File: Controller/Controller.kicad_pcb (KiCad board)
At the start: 4 copper layers, 65 x 56 mm, 62 parts, among them CN1 SERVO_PWM, CN10 FEMALE_LEFT, CN11 FEMALE_RIGHT, CN2 CFG1, CN3 CFG1, CN4 CFG1, CN5 FEMALE_LEFT, CN6 FEMALE_RIGHT, CN7 CFG1, CN8 CFG1, CN9 CFG1, J1 PJ-202AH, J10 ICSP, J11 MotorTerm, J12 MotorHeader, J13 MotorTerm, J14 MotorHeader, J15 UJ2-BH-1-TH, J2 TermLaser, J3 TermStop, J4 LASER_PWR, J5 LASER_PULSE, J6 TermControl, J7 TermLimit, J8 TermAux, J9 ConnPi, K1 SW_RESET, U1 CJ7805, U2 INTERFACE-CH340T_SSOP20_, U3 MCU-ATMEGA328P-AU_TQFP32_, Y1 12MHz, Y2 16MHZ

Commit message: Probably giving up on Pi option
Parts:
- J15: footprint UJ2-BH-1-TH:CUI_UJ2-BH-1-TH -> CUI:CUI_UJ2-BH-1-TH
- moved J10 229.9 mm to (96.5, 47.6)
- moved R1 200.7 mm to (59.1, 105.6)
- moved CN1 200.7 mm to (52.6, 106.4)
- moved J3 200.7 mm to (36.9, 92.2)
- moved J4 200.7 mm to (63.0, 90.1)
- moved J5 200.7 mm to (63.0, 94.1)
- moved J6 200.7 mm to (49.5, 92.2)
- moved J7 200.7 mm to (37.8, 100.4)
- moved J8 200.7 mm to (37.8, 108.7)
- moved C5 198.8 mm to (114.8, 91.4), turned to 90 degrees
- moved C3 196.3 mm to (106.9, 91.4), turned to 90 degrees
- moved C7 196.0 mm to (108.4, 56.9)
- moved R3 196.0 mm to (107.9, 61.8)
- moved C11 196.0 mm to (98.9, 67.4)
- moved C4 196.0 mm to (84.2, 70.8)
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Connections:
- J11 pad 1: Net-(CN6-Pad3) -> Net-(CN6-Pad6)
- J11 pad 2: Net-(CN6-Pad4) -> Net-(CN6-Pad5)
- J11 pad 3: Net-(CN6-Pad5) -> Net-(CN6-Pad4)
- J11 pad 4: Net-(CN6-Pad6) -> Net-(CN6-Pad3)
- J12 pad 1: Net-(CN6-Pad3) -> Net-(CN6-Pad6)
- J12 pad 2: Net-(CN6-Pad4) -> Net-(CN6-Pad5)
- J12 pad 3: Net-(CN6-Pad5) -> Net-(CN6-Pad4)
- J12 pad 4: Net-(CN6-Pad6) -> Net-(CN6-Pad3)
- J13 pad 1: Net-(CN11-Pad3) -> Net-(CN11-Pad6)
- J13 pad 2: Net-(CN11-Pad4) -> Net-(CN11-Pad5)
- J13 pad 3: Net-(CN11-Pad5) -> Net-(CN11-Pad4)
- J13 pad 4: Net-(CN11-Pad6) -> Net-(CN11-Pad3)
- J14 pad 1: Net-(CN11-Pad3) -> Net-(CN11-Pad6)
- J14 pad 2: Net-(CN11-Pad4) -> Net-(CN11-Pad5)
- J14 pad 3: Net-(CN11-Pad5) -> Net-(CN11-Pad4)
- J14 pad 4: Net-(CN11-Pad6) -> Net-(CN11-Pad3)
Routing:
- net GND: track 0.00 -> 35.2 mm
- net Net-(J15-Pad3): track 0.00 -> 10.4 mm
- net Net-(C3-Pad2): track 0.00 -> 9.46 mm
- net /VIN_12V: track 0.00 -> 9.07 mm
- net Net-(J15-Pad2): track 0.00 -> 7.28 mm
- net Net-(C5-Pad2): track 0.00 -> 6.24 mm
- net 5V: track 0.00 -> 2.63 mm
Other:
- net class 5V: via_dia 0.8 -> 1.2; via_drill 0.4 -> 0.6

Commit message: More power routing
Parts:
- removed J9: ConnPi, Connector_PinHeader_2.54mm:PinHeader_1x05_P2.54mm_Vertical
- added D3: LED_BLUE, OPL_Optoelectronics:LED-0603, F.Cu at (210.2, 35.6)
- added R7: 220R, OPL_Resistor:R0603, F.Cu at (210.2, 32.4)
- moved H1 150.9 mm to (215.9, 34.3)
- moved J3 142.1 mm to (172.3, 49.4), turned to 180 degrees
- moved J1 133.4 mm to (209.6, 59.7), turned to 270 degrees
- moved C1 123.3 mm to (203.5, 55.9), turned to 270 degrees
- moved U1 112.4 mm to (198.6, 58.9), turned to 270 degrees
- moved C4 111.5 mm to (193.4, 48.1), turned to 180 degrees
- moved D2 107.9 mm to (205.1, 35.6), turned to 270 degrees
- moved C2 104.9 mm to (193.8, 55.9), turned to 270 degrees
- moved D1 103.8 mm to (207.6, 35.6), turned to 270 degrees
- moved Y2 99.6 mm to (180.3, 35.4), turned to 180 degrees
- moved R5 98.7 mm to (207.6, 32.4), turned to 90 degrees
- moved U2 97.4 mm to (198.5, 42.5)
- moved Y1 97.1 mm to (198.5, 50.0)
- moved J15 97.1 mm to (205.5, 43.8)
- moved C3 96.6 mm to (194.6, 50.8)
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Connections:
- J3 pad 1: /GRBL_ABORT -> /NANO_RESET
- J3 pad 3: /NANO_RESET -> /GRBL_ABORT
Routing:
- net GND: track 35.2 -> 163.3 mm, vias 0 -> 4
- net 5V: track 2.63 -> 64.4 mm, vias 0 -> 4
- net /NANO_RESET: track 0.00 -> 16.7 mm
- net Net-(C12-Pad1): track 0.00 -> 6.43 mm, vias 0 -> 3
- net /GRBL_RX: track 0.00 -> 6.37 mm
- net /Arduino Nano/USB_RX: track 0.00 -> 6.32 mm
- net Net-(C8-Pad2): track 0.00 -> 5.96 mm
- net Net-(C7-Pad1): track 0.00 -> 5.94 mm
- net /GRBL_TX: track 0.00 -> 5.55 mm
- net Net-(C4-Pad1): track 0.00 -> 5.27 mm
- net /Arduino Nano/USB_TX: track 0.00 -> 5.04 mm
- net Net-(D3-Pad1): track 0.00 -> 1.65 mm
- net Net-(D2-Pad1): track 0.00 -> 1.65 mm
- net Net-(D1-Pad1): track 0.00 -> 1.65 mm
- net Net-(C3-Pad2): track 9.46 -> 8.31 mm
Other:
- board outline removed
- board text added: "PWR"
- board text added: "RX"
- board text added: "TX"

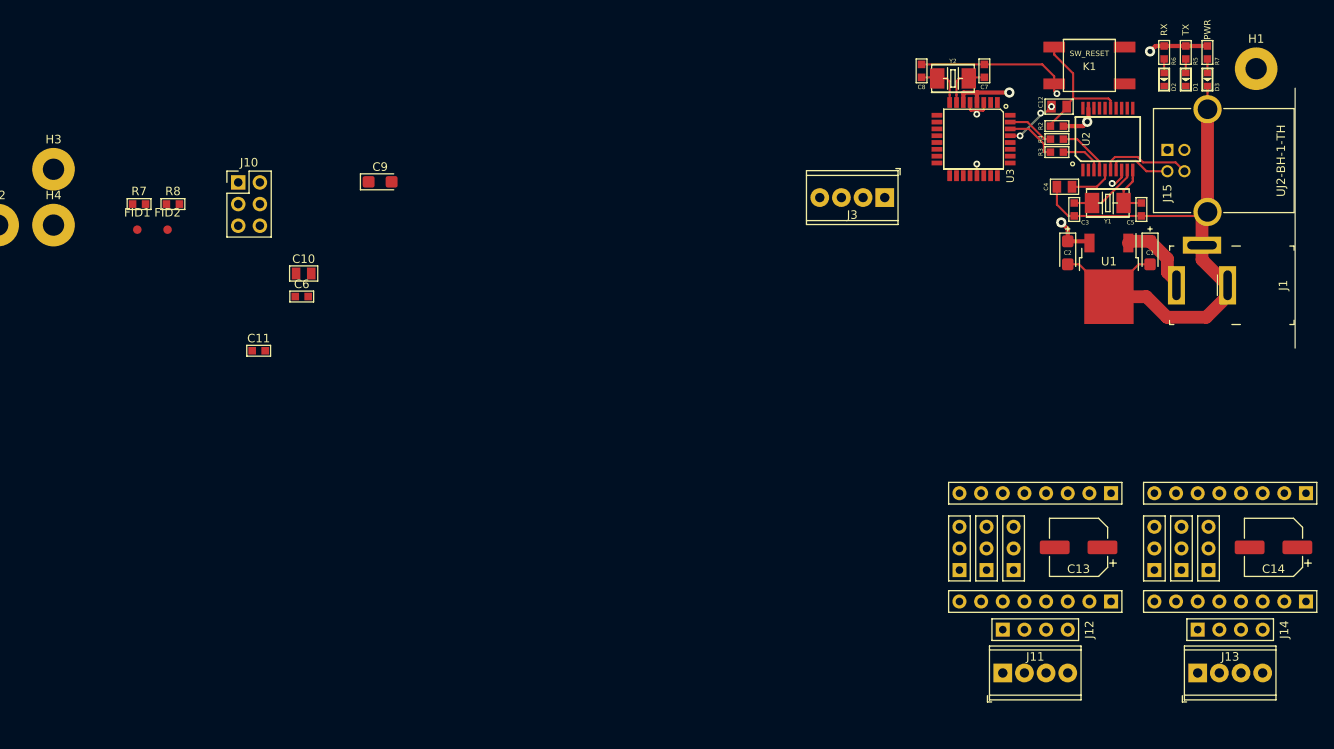
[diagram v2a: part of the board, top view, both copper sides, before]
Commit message: power and nano cleanup
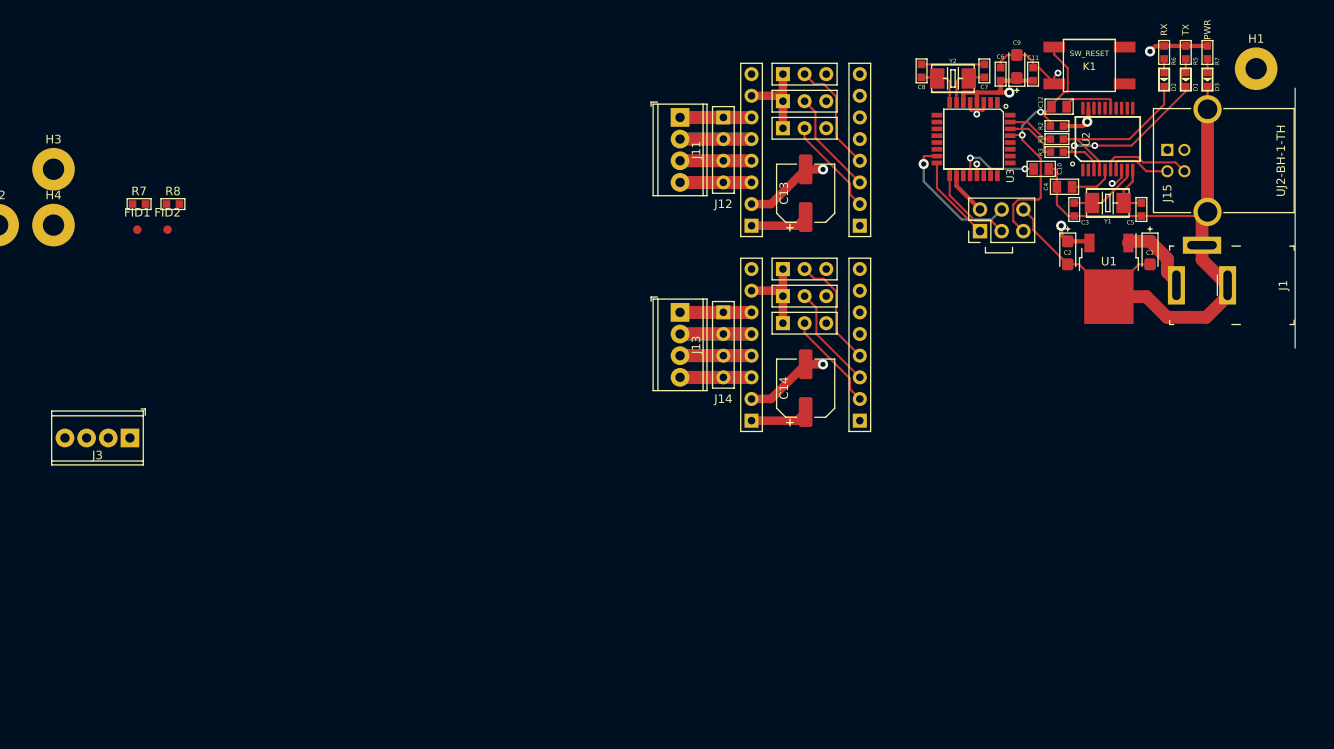
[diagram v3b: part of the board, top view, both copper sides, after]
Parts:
- moved C11 96.4 mm to (189.7, 34.9), turned to 270 degrees
- moved J3 92.9 mm to (83.8, 77.6)
- moved C10 87.4 mm to (190.7, 46.0)
- moved J10 87.2 mm to (183.5, 53.3), turned to 90 degrees
- moved C6 86.0 mm to (185.9, 34.9), turned to 270 degrees
- moved C9 75.9 mm to (187.8, 34.0), turned to 90 degrees
- moved J11 75.3 mm to (148.3, 40.0), turned to 270 degrees
- moved J13 74.0 mm to (148.3, 62.9), turned to 270 degrees
- moved J14 68.2 mm to (153.4, 66.7), turned to 90 degrees
- moved J12 67.1 mm to (153.4, 43.8), turned to 90 degrees
- moved CN11 63.7 mm to (156.7, 66.7), turned to 270 degrees
- moved CN6 62.5 mm to (156.7, 43.8), turned to 270 degrees
- moved CN4 58.5 mm to (162.9, 34.9), turned to 180 degrees
- moved C14 58.0 mm to (163.1, 71.8), turned to 90 degrees
- moved CN3 56.6 mm to (162.9, 38.1), turned to 180 degrees
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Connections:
- C12 pad 1: Net-(C12-Pad1) -> /NANO_RESET
- C12 pad 2: /NANO_RESET -> Net-(C12-Pad2)
- U2 pad 15: /NANO_RESET -> Net-(C12-Pad2)
- U3 pad 29: Net-(C12-Pad1) -> /NANO_RESET
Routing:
- net GND: track 163.3 -> 238.3 mm, vias 4 -> 6
- net 5V: track 64.4 -> 105.6 mm
- net /Arduino Nano/USB_TX: track 5.04 -> 22.3 mm, vias 0 -> 2
- net Net-(CN6-Pad6): track 0.00 -> 16.8 mm
- net Net-(CN6-Pad5): track 0.00 -> 16.8 mm
- net Net-(CN6-Pad4): track 0.00 -> 16.8 mm
- net Net-(CN6-Pad3): track 0.00 -> 16.8 mm
- net Net-(CN11-Pad6): track 0.00 -> 16.8 mm
- net Net-(CN11-Pad5): track 0.00 -> 16.8 mm
- net Net-(CN11-Pad4): track 0.00 -> 16.8 mm
- net Net-(CN11-Pad3): track 0.00 -> 16.8 mm
- net /NANO_RESET: track 16.7 -> 33.0 mm, vias 0 -> 2
- net /PULSE: track 0.00 -> 15.9 mm, vias 0 -> 1
- net /Arduino Nano/USB_RX: track 6.32 -> 22.0 mm
- net /VIN_12V: track 9.07 -> 22.6 mm
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
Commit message: Mostly final layout
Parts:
- removed the R7 at (84.9, 50.2)
- removed R8: 2K, OPL_Resistor:R0603
- moved J6 153.6 mm to (202.6, 79.4)
- moved H4 144.6 mm to (216.5, 81.5)
- moved CN1 136.0 mm to (182.2, 65.4)
- moved R1 134.7 mm to (183.6, 54.2), turned to 90 degrees
- moved J8 131.9 mm to (166.4, 79.4)
- moved J2 130.5 mm to (178.4, 79.4)
- moved J5 123.8 mm to (184.8, 71.8), turned to 90 degrees
- moved FID2 122.9 mm to (210.0, 70.0)
- moved J7 118.4 mm to (154.3, 79.4)
- moved J4 118.2 mm to (179.7, 71.8), turned to 90 degrees
- moved J3 106.7 mm to (190.5, 79.4), turned to 0 degrees
- moved H2 85.2 mm to (148.5, 81.5)
- moved H3 75.1 mm to (148.5, 31.5)
- moved FID1 65.4 mm to (150.0, 51.0)
- moved J10 6.08 mm to (178.2, 50.4), turned to 0 degrees
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- renumbered J15 to J9
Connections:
- J6 pad 1: /START -> /HOLD
- J6 pad 3: /HOLD -> /START
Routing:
- net GND: track 238.3 -> 364.7 mm, vias 6 -> 8
- net /X_LIMIT: track 0.00 -> 58.3 mm
- net /Y_LIMIT: track 0.00 -> 52.2 mm
- net /START: track 0.00 -> 44.0 mm
- net /HOLD: track 0.00 -> 39.6 mm
- net /GRBL_ABORT: track 0.00 -> 37.0 mm
- net /STEP_EN: track 0.00 -> 36.2 mm
- net /NANO_RESET: track 33.0 -> 66.3 mm, vias 2 -> 3
- net /PULSE: track 15.9 -> 48.9 mm, vias 1 -> 0
- net /Y_STEP: track 0.00 -> 32.1 mm, vias 0 -> 1
- net /X_STEP: track 0.00 -> 27.2 mm
- net /Y_DIR: track 0.00 -> 19.3 mm
- net /X_DIR: track 0.00 -> 12.1 mm
- net 5V: track 105.6 -> 111.9 mm, vias 4 -> 5
- net /Arduino Nano/D12: track 10.1 -> 5.19 mm
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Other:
- board outline added: 75 x 57 mm
- board text added: "12V"
- board text added: "5V"
- board text added: "ABORT"
- board text added: "AUX POWER"
- board text added: "CONTROL"
- board text added: "G"
- board text added: "GND"
- board text added: "HOLD"
- board text added: "LASER"
- board text added: "LIMITS"
- board text added: "PWM"
- board text added: "RESET"
- board text added: "SERVO"
- board text added: "START"
- board text added: "X"
- board text added: "Y"

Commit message: Near complete layout
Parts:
- moved H1 0.35 mm to (216.8, 31.2)
- moved H2 0.35 mm to (148.2, 81.8)
- moved H3 0.35 mm to (148.2, 31.2)
- moved H4 0.35 mm to (216.8, 81.8)
- moved C8 0.25 mm to (176.4, 34.5)
- moved C7 0.25 mm to (184.3, 34.5)
- moved J12 0.13 mm to (155.4, 40.0)
- moved J14 0.13 mm to (155.4, 61.6)
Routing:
- net GND: track 364.7 -> 529.1 mm
- net /VIN_12V: track 22.6 -> 120.8 mm
- net 5V: track 111.9 -> 171.2 mm
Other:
- board text added: "A+"
- board text added: "A-"
- board text added: "B+"
- board text added: "B-"
- board text added: "X MOTOR"
- board text added: "Y MOTOR"

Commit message: Beta v1
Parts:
- added G***: LOGO, Logos:logo_MLlabs_small, F.Cu at (190.5, 60.0)
- added J15: 12V_TERM, OPL_Connector:H2-5.0-10.5X8.0MM, F.Cu at (215.8, 70.5)
- moved FID2 5.83 mm to (205.0, 73.0)
- moved CN2 0.51 mm to (164.3, 37.5)
- moved CN3 0.51 mm to (164.3, 34.3)
- moved CN4 0.51 mm to (164.3, 31.1)
- moved CN7 0.51 mm to (164.3, 59.1)
- moved CN8 0.51 mm to (164.3, 55.9)
- moved CN9 0.51 mm to (164.3, 52.7)
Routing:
- net /VIN_12V: track 120.8 -> 152.1 mm
- net GND: track 529.1 -> 543.5 mm
- net /StepDriverY/CFG3: track 13.5 -> 14.6 mm
- net /StepDriverX/CFG3: track 13.5 -> 14.3 mm
- net 5V: track 171.2 -> 170.4 mm
- added copper zone on PWR, net /VIN_12V
- added copper zone on PWR, net 5V
- added copper zone on GND, net GND
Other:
- board text added: "1"
- board text added: "2"
- board text added: "3"
- board text added: "Laser Controller"
- board text added: "Maniacal Labs"
- board text added: "Platypus"
- board text added: "V"
